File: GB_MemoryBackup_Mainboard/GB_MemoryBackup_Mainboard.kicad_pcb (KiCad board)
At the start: 2 copper layers, 55.5 x 104.5 mm, 16 parts, among them J1 GB_Cart_EdgeConn-1Row-32Pins, J2 GB_Cart_Slot-1Row-32Pins, J3 JTAG-A, SW1 SW_SPDT, U1 AT29C010A-PLCC32, U2 28SF040-120-4C-NH-PLCC32, U3 Generic-ATF15xx-PLCC44

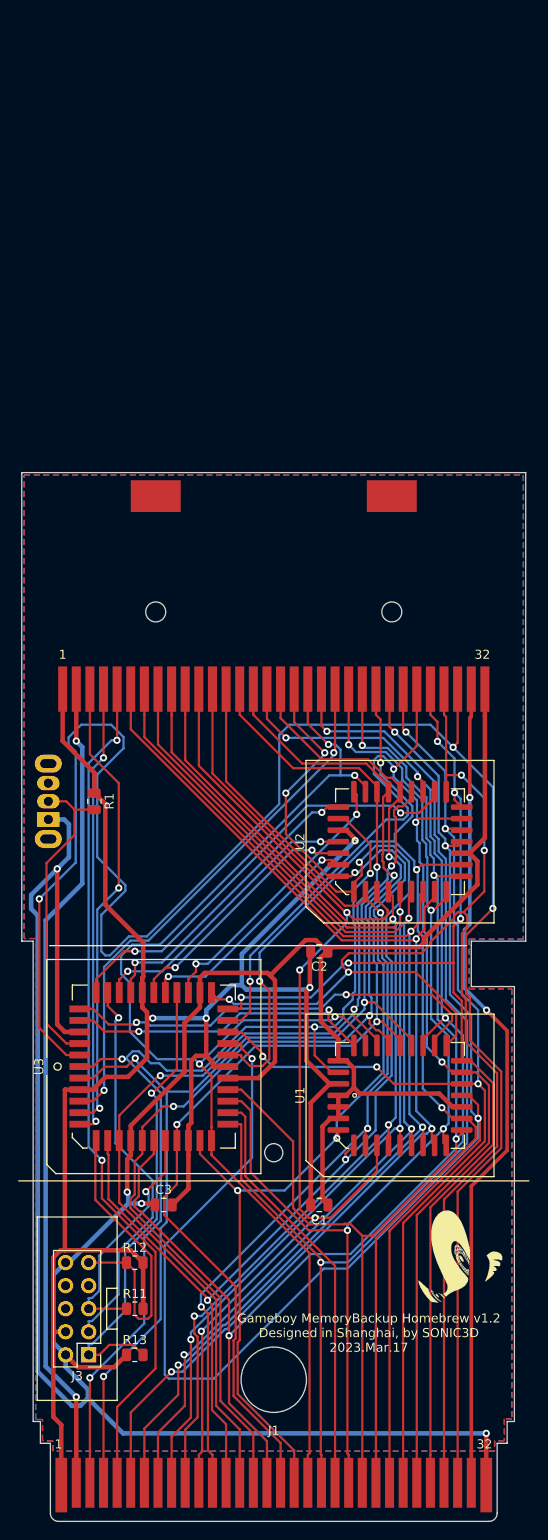
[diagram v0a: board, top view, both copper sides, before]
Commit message: Modified: PCB for v1.3 schematic.(Unrouted yet.)
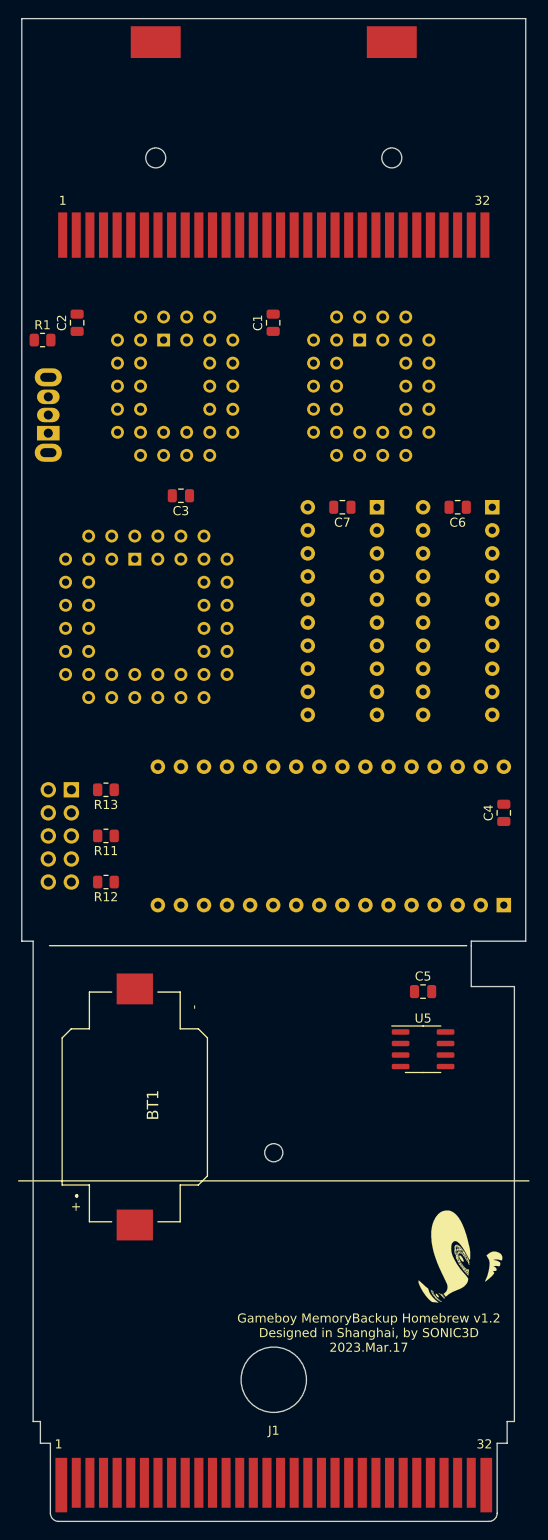
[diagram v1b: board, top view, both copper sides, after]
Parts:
- removed the G*** at (68.5, 50.8)
- added BT1: 3V, Battery_JLCPCB:BAT-SMD_CR1616, F.Cu at (74.3, 109.9)
- added C4: 0.1uF, Capacitor_SMD:C_0805_2012Metric, F.Cu at (114.9, 77.5)
- added C5: 0.1uF, Capacitor_SMD:C_0805_2012Metric, F.Cu at (106.0, 97.2)
- added C6: 0.1uF, Capacitor_SMD:C_0805_2012Metric, F.Cu at (109.9, 43.8)
- added C7: 0.1uF, Capacitor_SMD:C_0805_2012Metric, F.Cu at (97.2, 43.8)
- added U4: TC551001BPL_DIP32, Package_DIP:DIP-32_W15.24mm_Socket, B.Cu at (114.9, 87.6)
- added U5: BA6162F, Package_SO:SOIC-8_3.9x4.9mm_P1.27mm, F.Cu at (106.0, 103.5)
- added U6: 74HC373, Package_DIP:DIP-20_W7.62mm_Socket, B.Cu at (113.7, 43.8)
- added U7: 74HC373, Package_DIP:DIP-20_W7.62mm_Socket, B.Cu at (101.0, 43.8)
- J3: moved to B.Cu
- U1, U2: footprint Package_LCC_JLCPCB:PLCC-32_L14.0-W11.5-P1.27-T -> Package_LCC_JLCPCB:PLCC-32_THT-Socket; moved to B.Cu
- U3: footprint Package_LCC_JLCPCB:LCC-44_L23.2-W23.2-P1.27-T -> Package_LCC_JLCPCB:PLCC-44_THT-Socket; moved to B.Cu
- moved C1 97.3 mm to (89.5, 23.5), turned to 90 degrees
- moved U1 83.3 mm to (99.1, 25.4), turned to 180 degrees
- moved C3 78.1 mm to (79.4, 42.5), turned to 180 degrees
- moved C2 74.2 mm to (67.9, 23.5), turned to 90 degrees
- moved R13 62.3 mm to (71.1, 74.9), turned to 180 degrees
- moved J3 62.3 mm to (67.3, 74.9)
- moved U2 61.1 mm to (77.5, 25.4), turned to 180 degrees
- moved U3 55.9 mm to (74.3, 49.5), turned to 180 degrees
- moved R11 52.2 mm to (71.1, 80.0), turned to 180 degrees
- moved R1 51.1 mm to (64.1, 25.4), turned to 0 degrees
- moved J2 50.0 mm to (89.6, 3.59)
- moved SW1 42.5 mm to (64.8, 33.7)
- moved R12 42.0 mm to (71.1, 85.1), turned to 180 degrees
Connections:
- U1 pad 1: GND -> /F010_A18
- U1 pad 2: GND -> /F010_A16
- U1 pad 3: GND -> /F010_A15
- U1 pad 30: GND -> /F010_A17
- U3 pad 31: /F040_A14 -> /HC373_010_LE
- U3 pad 33: /F040_A15 -> /HC373_040_LE
- U3 pad 34: /F040_A16 -> /RAM_A16
- U3 pad 36: /F040_A17 -> /RAM_A15
- U3 pad 37: /F040_A18 -> /RAM_A14
- U3 pad 41: /F010_A14 -> /~RAM_CE
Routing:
- net GND: track 330.3 -> 0.00 mm, vias 4 -> 0
- net /~ARST: track 223.3 -> 0.00 mm, vias 3 -> 0
- net +5V: track 216.2 -> 0.00 mm, vias 4 -> 0
- net /AD3: track 191.6 -> 0.00 mm, vias 4 -> 0
- net /AA10: track 150.4 -> 0.00 mm, vias 4 -> 0
- net /AD7: track 149.8 -> 0.00 mm, vias 4 -> 0
- net /AD5: track 146.5 -> 0.00 mm, vias 4 -> 0
- net /AA7: track 143.0 -> 0.00 mm, vias 3 -> 0
- net /AD2: track 141.9 -> 0.00 mm, vias 4 -> 0
- net /AA13: track 139.0 -> 0.00 mm, vias 4 -> 0
- net /AA0: track 129.0 -> 0.00 mm, vias 3 -> 0
- net /AA8: track 128.9 -> 0.00 mm, vias 3 -> 0
- net /AA9: track 128.7 -> 0.00 mm, vias 3 -> 0
- net /AD1: track 128.4 -> 0.00 mm, vias 3 -> 0
- net /AD4: track 126.9 -> 0.00 mm, vias 5 -> 0
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- removed copper zone on F.Cu, net +5V
- removed copper zone on B.Cu, net GND
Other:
- board size 55.5 x 104.5 mm -> 55.5 x 154.5 mm

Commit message: Modified: PCB with Subboard-A slot.(Unrouted yet.)
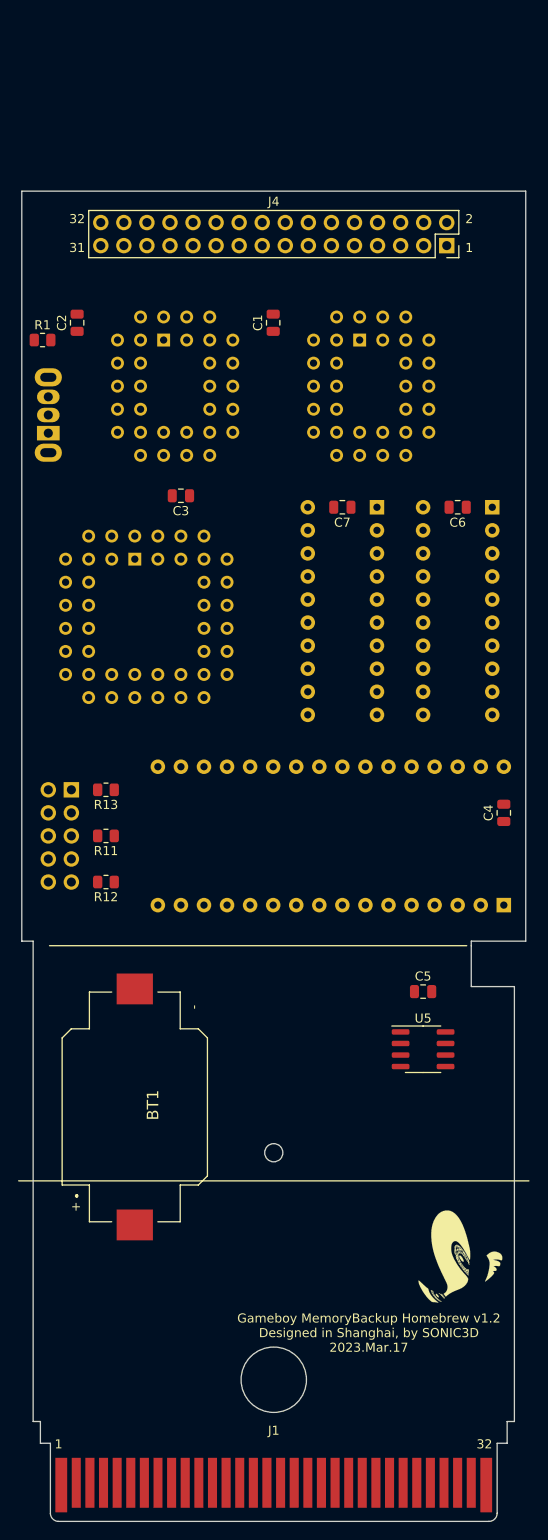
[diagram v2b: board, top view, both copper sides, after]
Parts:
- removed J2: GB_Cart_Slot-1Row-32Pins, NintendoGBCart_ExtFootprint:GB_GBA_Cartridge_Slot
- added J4: Conn_02x16_Odd_Even, Connector_PinSocket_2.54mm:PinSocket_2x16_P2.54mm_Vertical, F.Cu at (108.7, 15.0)
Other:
- board size 55.5 x 154.5 mm -> 55.5 x 135.5 mm
- board text added: "1"
- board text added: "2"
- board text added: "31"
- board text added: "32"

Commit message: Modified: PCB components position modified for easier track routing.
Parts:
- moved J4 78.9 mm to (70.5, 84.1), turned to 90 degrees
- moved C1 9.67 mm to (93.3, 14.6)
- moved U1 9.67 mm to (102.9, 16.5)
- moved C2 8.89 mm to (67.9, 14.6)
- moved C3 8.89 mm to (79.4, 33.7)
- moved C4 8.89 mm to (114.9, 68.6)
- moved C6 8.89 mm to (109.9, 34.9)
- moved C7 8.89 mm to (97.2, 34.9)
- moved J3 8.89 mm to (67.3, 66.0)
- moved R11 8.89 mm to (71.1, 71.1)
- moved R12 8.89 mm to (71.1, 76.2)
- moved R13 8.89 mm to (71.1, 66.0)
- moved SW1 8.89 mm to (64.8, 24.8)
- moved U3 8.89 mm to (74.3, 40.6)
- moved U4 8.89 mm to (114.9, 78.7)
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
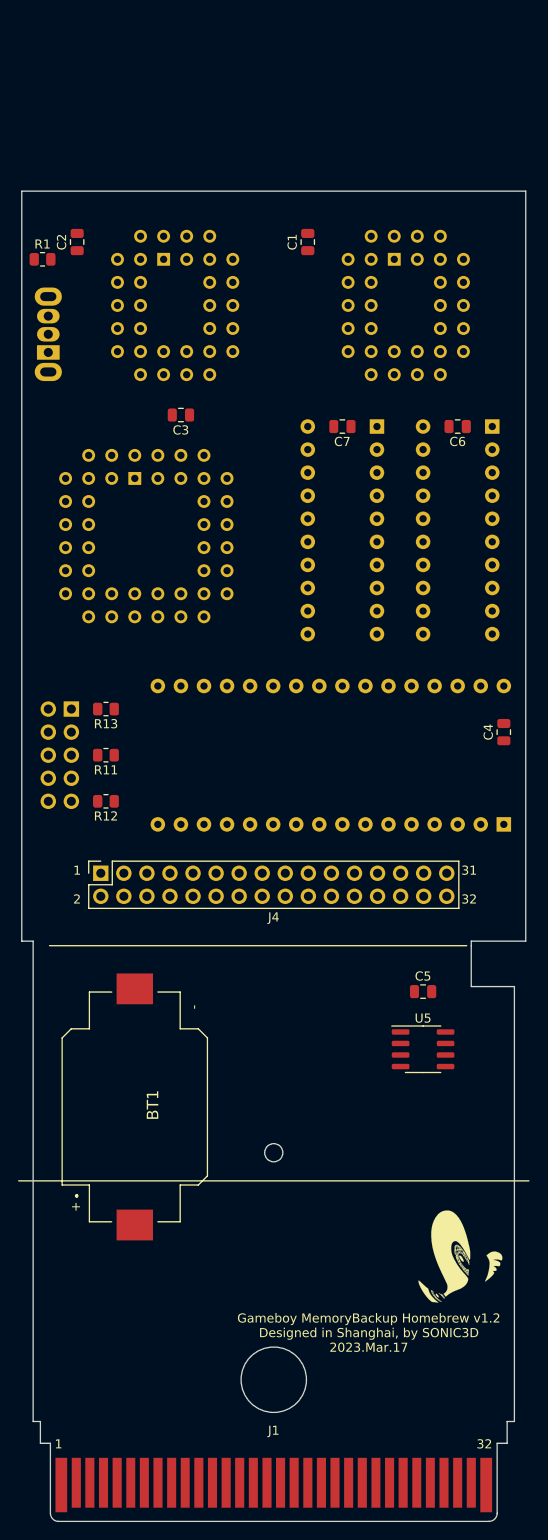
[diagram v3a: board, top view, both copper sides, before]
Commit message: Modified: PCB routed and manually revised. Modified: Added all info text labels on silk layers.
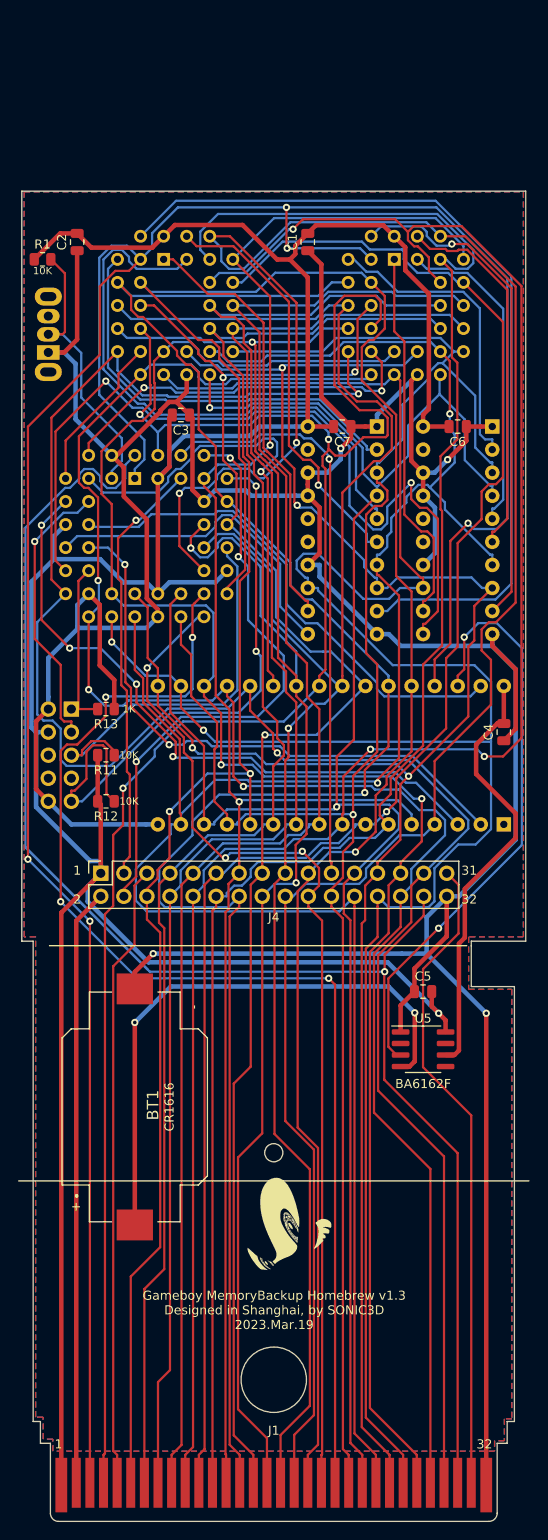
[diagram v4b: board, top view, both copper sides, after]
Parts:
- added G***: LOGO, LogoGraphics:MaskLayer_12mm_x_12mm_ShadowSonic, B.Cu at (88.3, 123.2)
- moved G*** 19.2 mm to (91.5, 122.9)
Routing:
- net GND: track 0.00 -> 425.4 mm, vias 0 -> 4
- net +5V: track 0.00 -> 336.5 mm, vias 0 -> 1
- net /~AWR: track 0.00 -> 288.3 mm, vias 0 -> 5
- net /AD4: track 0.00 -> 249.0 mm, vias 0 -> 2
- net /AA12: track 0.00 -> 246.5 mm, vias 0 -> 2
- net /AD2: track 0.00 -> 245.1 mm, vias 0 -> 2
- net /AD7: track 0.00 -> 224.3 mm, vias 0 -> 2
- net /AD1: track 0.00 -> 221.1 mm, vias 0 -> 2
- net /AD3: track 0.00 -> 220.7 mm, vias 0 -> 4
- net /AD0: track 0.00 -> 214.8 mm, vias 0 -> 1
- net /AA13: track 0.00 -> 212.6 mm, vias 0 -> 1
- net /AA4: track 0.00 -> 210.8 mm, vias 0 -> 3
- net /~ARD: track 0.00 -> 203.7 mm, vias 0 -> 3
- net /AA8: track 0.00 -> 203.2 mm, vias 0 -> 1
- net /AD6: track 0.00 -> 197.9 mm, vias 0 -> 3
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- added copper zone on F.Cu, net +5V
- added copper zone on B.Cu, net GND
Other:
- net class AudioLine: trace_width 0.4 -> 0.25
- board text added: "10K"
- board text added: "1K"
- board text added: "512KB_PRG_ROM"
- board text added: "512KB_STORAGE_ROM"
- board text added: "74HC373"
- board text added: "ATF1502/ATF1504"
- board text added: "BA6162F"
- board text added: "CR1616"
- board text added: "GND Vtgt x x GND"
- board text added: "Gameboy MemoryBackup Homebrew v1.3 Designed in Shanghai, by SONIC3D 2023.Mar.19"
- board text added: "Gameboy MemoryBackup Homebrew v1.3 https://github.com/SONIC3D/gameboy-memorybackup Designed in Shanghai, by SONIC3D 2023.Mar.19"
- board text added: "TC551001_128KB_RAM"
- board text added: "TCK TDO TMS x TDI"
- board text removed: "Gameboy MemoryBackup Homebrew v1.2 Designed in Shanghai, by SONIC3D 2023.Mar.17"
- board text removed: "Gameboy MemoryBackup Homebrew v1.2 https://github.com/SONIC3D/gameboy-memorybackup Designed in Shanghai, by SONIC3D 2023.Mar.17"
